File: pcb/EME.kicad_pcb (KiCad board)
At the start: 2 copper layers, 42 parts, among them J1 BMP180, J10 Reset, J11 UART0, J12 SPI_CONN, J13 UART2, J14 MQ135, J15 AS5600, J3 SS41, J4 Hoja Mojada, J5 PanelSolar, J6 BH1750, J7 DHT22, J8 Baterias, J9 Jumper, SW1 Enable, U1 LM78M05_TO220, U5 TL082

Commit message: se actualizó la PCB
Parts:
- removed J15: AS5600, Connector_PinHeader_2.54mm:PinHeader_1x05_P2.54mm_Vertical
- added D3: LED, LED_THT:LED_D5.0mm_Clear, F.Cu at (114.8, 93.2)
- added H4: Sujeción, MountingHole:MountingHole_3.2mm_M3_Pad_Via, F.Cu at (127.6, 24.4)
- added J16: OUT, Connector_PinHeader_2.54mm:PinHeader_1x03_P2.54mm_Vertical, F.Cu at (45.2, 69.3)
- added J17: OE, Connector_PinHeader_2.54mm:PinHeader_1x03_P2.54mm_Vertical, F.Cu at (39.0, 64.0)
- added J18: GPIO's, Connector_PinHeader_2.54mm:PinHeader_1x05_P2.54mm_Vertical, F.Cu at (84.8, 31.6)
- added J19: I2C, Connector_PinHeader_2.54mm:PinHeader_1x05_P2.54mm_Vertical, F.Cu at (108.5, 25.7)
- added J2: ReedSwitchX8, Connector_PinHeader_2.54mm:PinHeader_1x09_P2.54mm_Vertical, F.Cu at (35.9, 38.9)
- added J20: Jumper, Connector_PinHeader_2.54mm:PinHeader_1x02_P2.54mm_Vertical, F.Cu at (117.2, 88.1)
- added Q1: IRF540N, Package_TO_SOT_THT:TO-220-3_Vertical, F.Cu at (68.8, 89.5)
- added Q2: IRF540N, Package_TO_SOT_THT:TO-220-3_Vertical, F.Cu at (98.7, 27.0)
- added R10: 10k, Resistor_THT:R_Axial_DIN0207_L6.3mm_D2.5mm_P10.16mm_Horizontal, F.Cu at (42.4, 43.9)
- added R11: 10k, Resistor_THT:R_Axial_DIN0207_L6.3mm_D2.5mm_P10.16mm_Horizontal, F.Cu at (63.6, 57.0)
- added R12: 10k, Resistor_THT:R_Axial_DIN0207_L6.3mm_D2.5mm_P10.16mm_Horizontal, F.Cu at (45.4, 48.1)
- added R13: 10k, Resistor_THT:R_Axial_DIN0207_L6.3mm_D2.5mm_P10.16mm_Horizontal, F.Cu at (39.2, 50.9)
- added R14: 10k, Resistor_THT:R_Axial_DIN0207_L6.3mm_D2.5mm_P10.16mm_Horizontal, F.Cu at (42.4, 52.8)
- added R15: 10k, Resistor_THT:R_Axial_DIN0207_L6.3mm_D2.5mm_P10.16mm_Horizontal, F.Cu at (54.2, 69.2)
- added R17: 1k, Resistor_THT:R_Axial_DIN0207_L6.3mm_D2.5mm_P10.16mm_Horizontal, F.Cu at (73.5, 87.0)
- added R18: 4k7, Resistor_THT:R_Axial_DIN0207_L6.3mm_D2.5mm_P10.16mm_Horizontal, F.Cu at (70.0, 76.6)
- added R19: 4k7, Resistor_THT:R_Axial_DIN0207_L6.3mm_D2.5mm_P10.16mm_Horizontal, F.Cu at (78.5, 63.9)
- added R20: 1k, Resistor_THT:R_Axial_DIN0207_L6.3mm_D2.5mm_P10.16mm_Horizontal, F.Cu at (88.7, 70.2)
- added R21: 4k7, Resistor_THT:R_Axial_DIN0207_L6.3mm_D2.5mm_P10.16mm_Horizontal, F.Cu at (94.5, 28.2)
- added R22: 4k7, Resistor_THT:R_Axial_DIN0207_L6.3mm_D2.5mm_P10.16mm_Horizontal, F.Cu at (94.5, 25.1)
- added R23: 4k7, Resistor_THT:R_Axial_DIN0207_L6.3mm_D2.5mm_P10.16mm_Horizontal, F.Cu at (99.7, 35.5)
- added R24: 1k, Resistor_THT:R_Axial_DIN0207_L6.3mm_D2.5mm_P10.16mm_Horizontal, F.Cu at (120.5, 77.9)
- added R8: 10k, Resistor_THT:R_Axial_DIN0207_L6.3mm_D2.5mm_P10.16mm_Horizontal, F.Cu at (59.2, 53.7)
- added R9: 10k, Resistor_THT:R_Axial_DIN0207_L6.3mm_D2.5mm_P10.16mm_Horizontal, F.Cu at (39.4, 41.5)
- added U3: 74HC251, Package_DIP:DIP-16_W7.62mm_LongPads, F.Cu at (48.5, 47.8)
- H1, H2, H3: value Sujeción GND -> Sujeción
- J11: value UART0 -> UART2; footprint Connector_PinHeader_2.54mm:PinHeader_1x04_P2.54mm_Vertical -> Connector_PinHeader_2.54mm:PinHeader_1x05_P2.54mm_Vertical
- J13: value UART2 -> UART0; footprint Connector_PinHeader_2.54mm:PinHeader_1x04_P2.54mm_Vertical -> Connector_PinHeader_2.54mm:PinHeader_1x05_P2.54mm_Vertical
- J5: footprint TerminalBlock_Phoenix:TerminalBlock_Phoenix_MPT-0,5-2-2.54_1x02_P2.54mm_Horizontal -> TerminalBlock_Phoenix:TerminalBlock_Phoenix_PT-1,5-2-3.5-H_1x02_P3.50mm_Horizontal
- J8: footprint TerminalBlock_Phoenix:TerminalBlock_Phoenix_MPT-0,5-2-2.54_1x02_P2.54mm_Horizontal -> TerminalBlock_Phoenix:TerminalBlock_Phoenix_PT-1,5-2-5.0-H_1x02_P5.00mm_Horizontal
- moved H1 264.2 mm to (37.7, 24.5)
- moved R1 233.2 mm to (41.6, 73.8), turned to -90 degrees
- moved C5 218.1 mm to (40.1, 86.4), turned to 180 degrees
- moved RV1 217.3 mm to (35.9, 76.8)
- moved U5 217.0 mm to (44.9, 75.9)
- moved R2 216.9 mm to (55.8, 73.3)
- moved R4 213.3 mm to (42.8, 86.3)
- moved J3 212.7 mm to (51.1, 90.5)
- moved C7 209.6 mm to (58.8, 81.0), turned to 0 degrees
- moved R16 205.5 mm to (59.9, 30.1)
- moved J6 204.1 mm to (70.4, 33.9), turned to 180 degrees
- moved J1 196.3 mm to (74.9, 23.8), turned to 0 degrees
- moved J4 196.0 mm to (51.6, 26.8)
- moved J14 192.3 mm to (45.8, 33.7), turned to 180 degrees
- moved SW1 191.7 mm to (67.0, 25.5), turned to -90 degrees
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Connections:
- C5 pad 2: GNDREF -> GND_G1
- C6 pad 2: GNDREF -> GND_G1
- C7 pad 2: GNDREF -> GND_G1
- C9 pad 1: Net-(J10-Pin_2) -> Rest
- J1 pad 2: SDA -> SCL
- J1 pad 3: SCL -> SDA
- J1 pad 4: GNDREF -> GND_G1
- J10 pad 2: Net-(J10-Pin_2) -> Rest
- J11 pad 1: +3.3V -> GND_G2
- J11 pad 2: Net-(J11-Pin_2) -> RX2
- J11 pad 3: Net-(J11-Pin_3) -> TX2
- J11 pad 4: GNDREF -> +5V
- J12 pad 1: GNDREF -> SS
- J12 pad 2: Net-(J12-Pin_2) -> SCK
- J12 pad 3: Net-(J12-Pin_3) -> MOSI
- J12 pad 4: Net-(J12-Pin_4) -> MISO
- J12 pad 5: Net-(J12-Pin_5) -> GND_G2
- J12 pad 6: +3.3V -> +5V
- J12 pad 7: Net-(J12-Pin_7) -> +3.3V
- J13 pad 1: +3.3V -> GND_G2
- J13 pad 2: Net-(J13-Pin_2) -> RX0
- J13 pad 3: Net-(J13-Pin_3) -> TX0
- J13 pad 4: GNDREF -> +5V
- J14 pad 3: GNDREF -> GND_G1
- J3 pad 2: GNDREF -> GND_G1
- J4 pad 3: GNDREF -> GND_G1
- J6 pad 2: GNDREF -> GND_G1
- J6 pad 3: SCL -> SDA
- J6 pad 4: SDA -> SCL
- J7 pad 4: GNDREF -> GND_G1
- R16 pad 1: +3.3V -> Rest
- R16 pad 2: Net-(J10-Pin_2) -> +3.3V
- R4 pad 1: Net-(J3-Pin_3) -> Net-(U5A-+)
- R4 pad 2: Net-(U5A-+) -> Net-(J3-Pin_3)
- R5 pad 1: SDA -> SCL
- R6 pad 1: SCL -> SDA
- RV1 pad 3: GNDREF -> GND_G1
- SW1 pad 2: Net-(J10-Pin_2) -> Rest
- U2 pad 1: Net-(J10-Pin_2) -> Rest
- U2 pad 10: unconnected-(U2-D27/ADC2_7/T7/~-Pad10) -> G2
- U2 pad 11: unconnected-(U2-D14/ADC2_6/HSPI_CLK/T6/~-Pad11) -> G1
- U2 pad 12: unconnected-(U2-D12/ADC2_5/HSPI_Q/T5/~-Pad12) -> GPIO12
- U2 pad 13: unconnected-(U2-D13/ADC2_4/HSPI_ID/T4/~-Pad13) -> GPIO13
- U2 pad 20: Net-(J12-Pin_2) -> GPIO4
- U2 pad 21: Net-(J13-Pin_3) -> RX2
- U2 pad 22: Net-(J13-Pin_2) -> TX2
- U2 pad 23: Net-(J12-Pin_3) -> SS
- U2 pad 24: Net-(J12-Pin_4) -> SCK
- U2 pad 25: Net-(J12-Pin_5) -> MISO
- U2 pad 27: Net-(J11-Pin_2) -> RX0
- U2 pad 28: Net-(J11-Pin_3) -> TX0
- U2 pad 30: Net-(J12-Pin_7) -> MOSI
- U2 pad 6: Net-(J15-Pin_1) -> S0
- U2 pad 7: unconnected-(U2-D33/ADC1_5/T8/~-Pad7) -> S1
- U2 pad 8: unconnected-(U2-D25/ADC2_8/DAC1/~-Pad8) -> S2
- U2 pad 9: unconnected-(U2-D26/ADC2_9/DAC2/~-Pad9) -> Y
- U5 pad 4: GNDREF -> GND_G1
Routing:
- net +3.3V: track 276.4 -> 370.3 mm, vias 10 -> 8
- net GNDREF: track 17.4 -> 91.4 mm, vias 4 -> 8
- net +5V: track 86.0 -> 155.9 mm, vias 0 -> 4
- net GPIO13: track 0.00 -> 67.8 mm
- net GPIO12: track 0.00 -> 60.5 mm
- net GPIO4: track 0.00 -> 55.7 mm
- net Rest: track 0.00 -> 55.1 mm
- net DHT22: track 14.4 -> 63.5 mm, vias 0 -> 2
- net Net-(Q2-G): track 0.00 -> 48.8 mm
- net Net-(J12-Pin_7): track 45.0 -> 0.00 mm
- net Net-(J2-Pin_4): track 0.00 -> 44.8 mm, vias 0 -> 4
- net Net-(J2-Pin_1): track 0.00 -> 42.4 mm
- net SS: track 0.00 -> 40.0 mm
- net SCK: track 0.00 -> 36.4 mm
- net MQ135_Dg: track 8.42 -> 44.6 mm
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- added copper zone on B.Cu, net GND_G1
- added copper zone on B.Cu, net GND_G2
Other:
- board outline added: 100 x 78 mm
- board text added: "EMETec UM"
- board text added: "v:1.8 f:21/10/24"
- board text removed: "EME ETec UM"
- board text removed: "v:1.0 f:16/06/24"

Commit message: se actualizó la PCB
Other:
- board text added: "v:1.8.2 f:27/10/24"
- board text removed: "v:1.8 f:21/10/24"

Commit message: update main
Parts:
- J5: footprint TerminalBlock_Phoenix:TerminalBlock_Phoenix_PT-1,5-2-3.5-H_1x02_P3.50mm_Horizontal -> TerminalBlock_Phoenix:TerminalBlock_Phoenix_PT-1,5-2-5.0-H_1x02_P5.00mm_Horizontal
- moved J12 3.40 mm to (128.9, 40.0)
- moved J5 0.76 mm to (127.5, 51.5)
- moved C3 0.75 mm to (121.0, 91.0)
- moved C4 0.33 mm to (116.2, 78.5)
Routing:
- net MISO: track 32.1 -> 34.6 mm
- net SCK: track 36.4 -> 38.6 mm
- net SS: track 40.0 -> 42.1 mm
- net MOSI: track 30.9 -> 32.9 mm
- net GNDREF: track 91.4 -> 90.2 mm
- net +3.3V: track 370.3 -> 371.3 mm
- net +5V: track 155.9 -> 156.9 mm
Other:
- board text added: "f:02/11/24"
- board text added: "v:1.8.3"
- board text removed: "v:1.8.2 f:27/10/24"

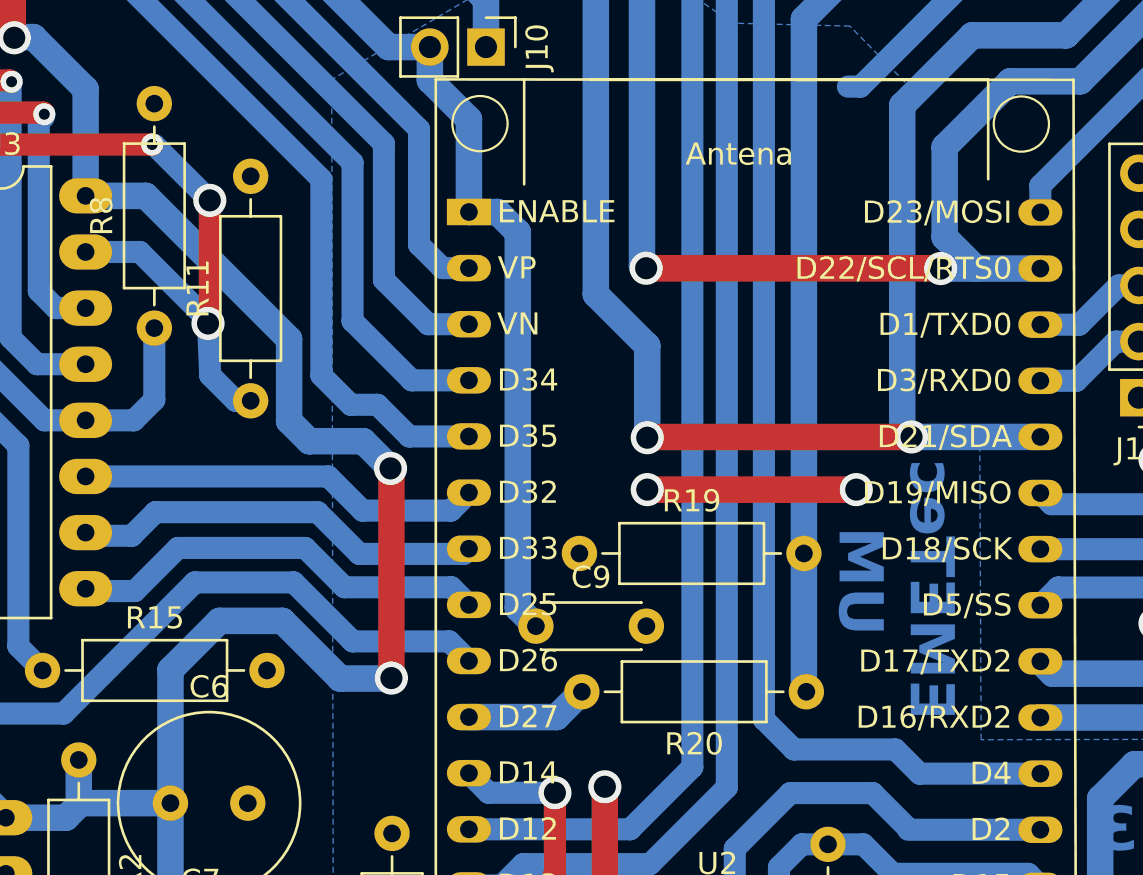
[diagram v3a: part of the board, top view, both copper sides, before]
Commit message: Se actualizó PCB y se agregó funcionalidad de sensor lluvia, veleta y anemómetro
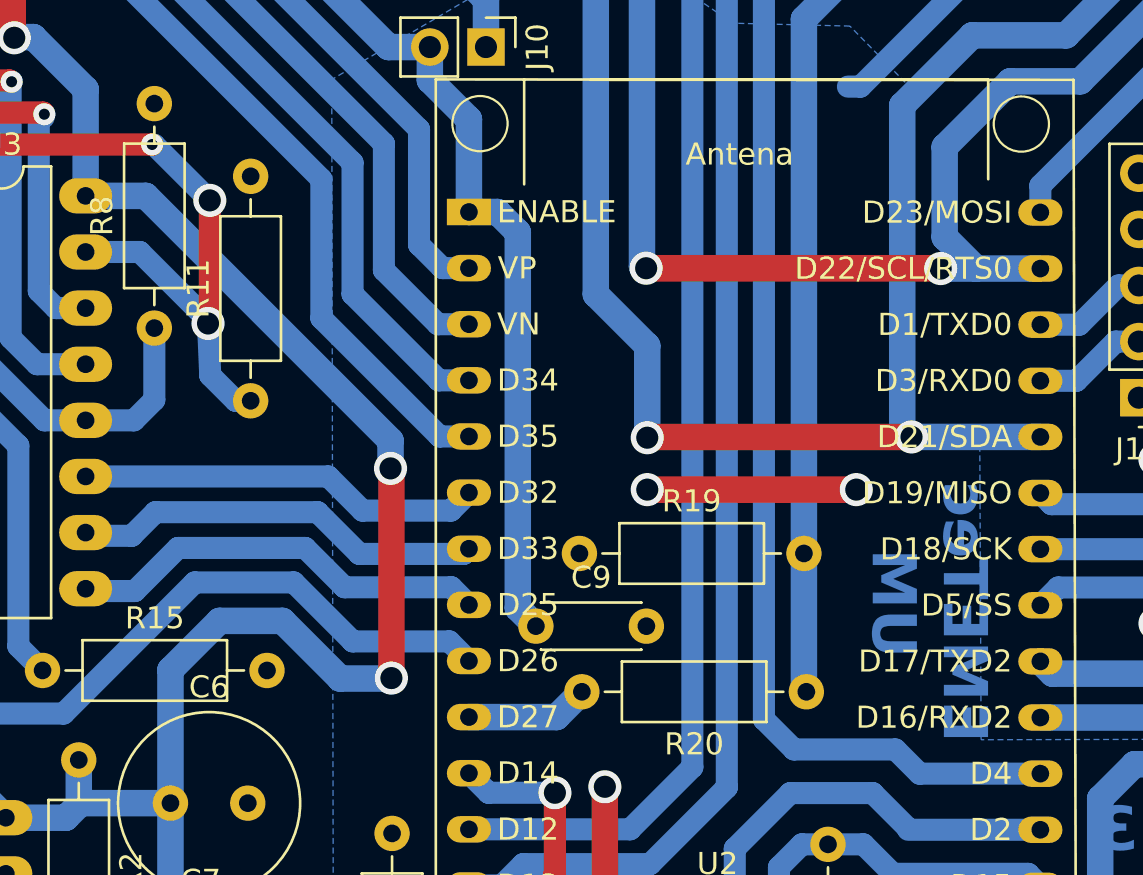
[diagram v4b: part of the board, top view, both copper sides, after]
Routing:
- net MQ135_An: track 43.2 -> 41.7 mm
- net +3.3V: track 371.3 -> 369.9 mm
- net MQ135_Dg: track 44.6 -> 43.9 mm

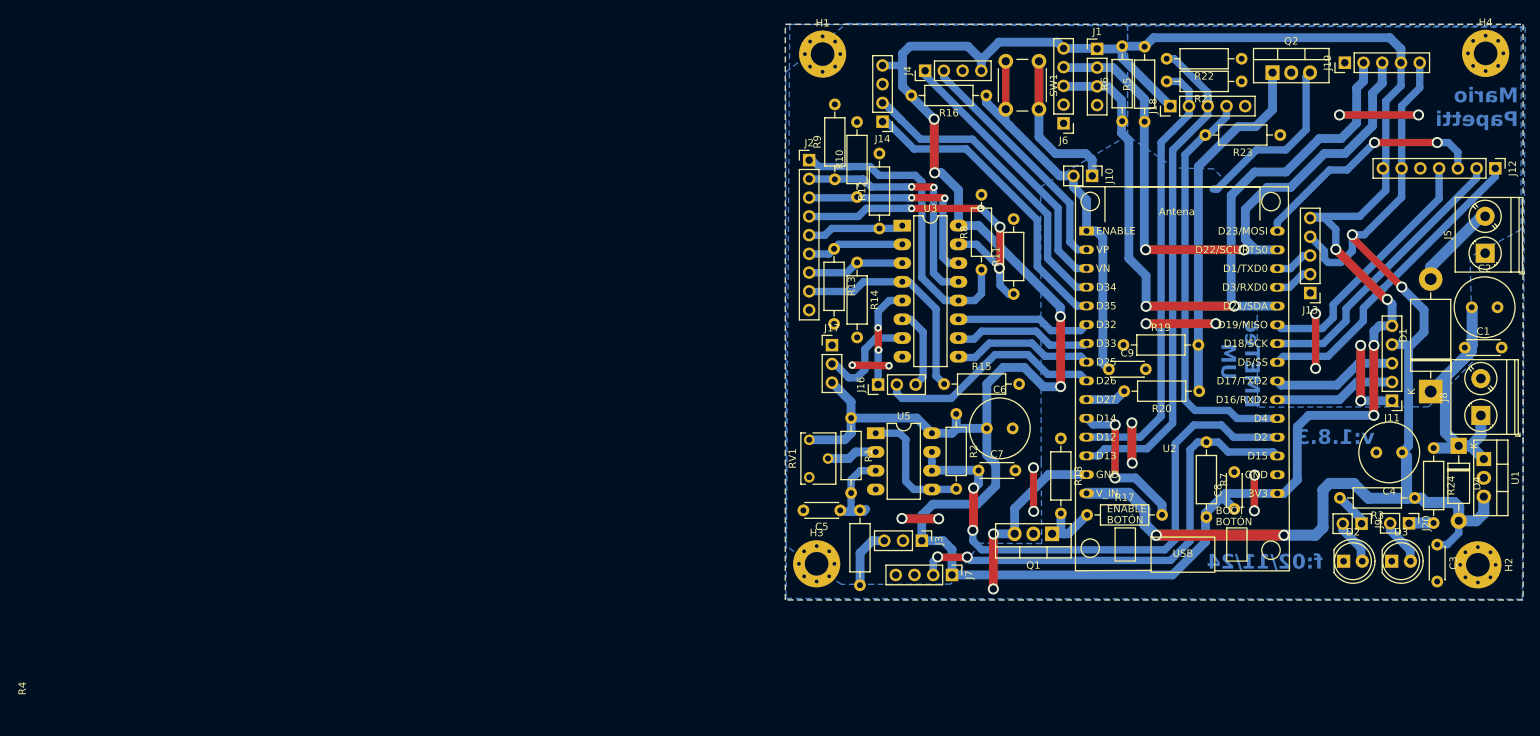
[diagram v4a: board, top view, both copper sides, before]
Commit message: Nueva versión de la PCB, se saca a parte veleta y anemómetro en placas aparte con los sensores
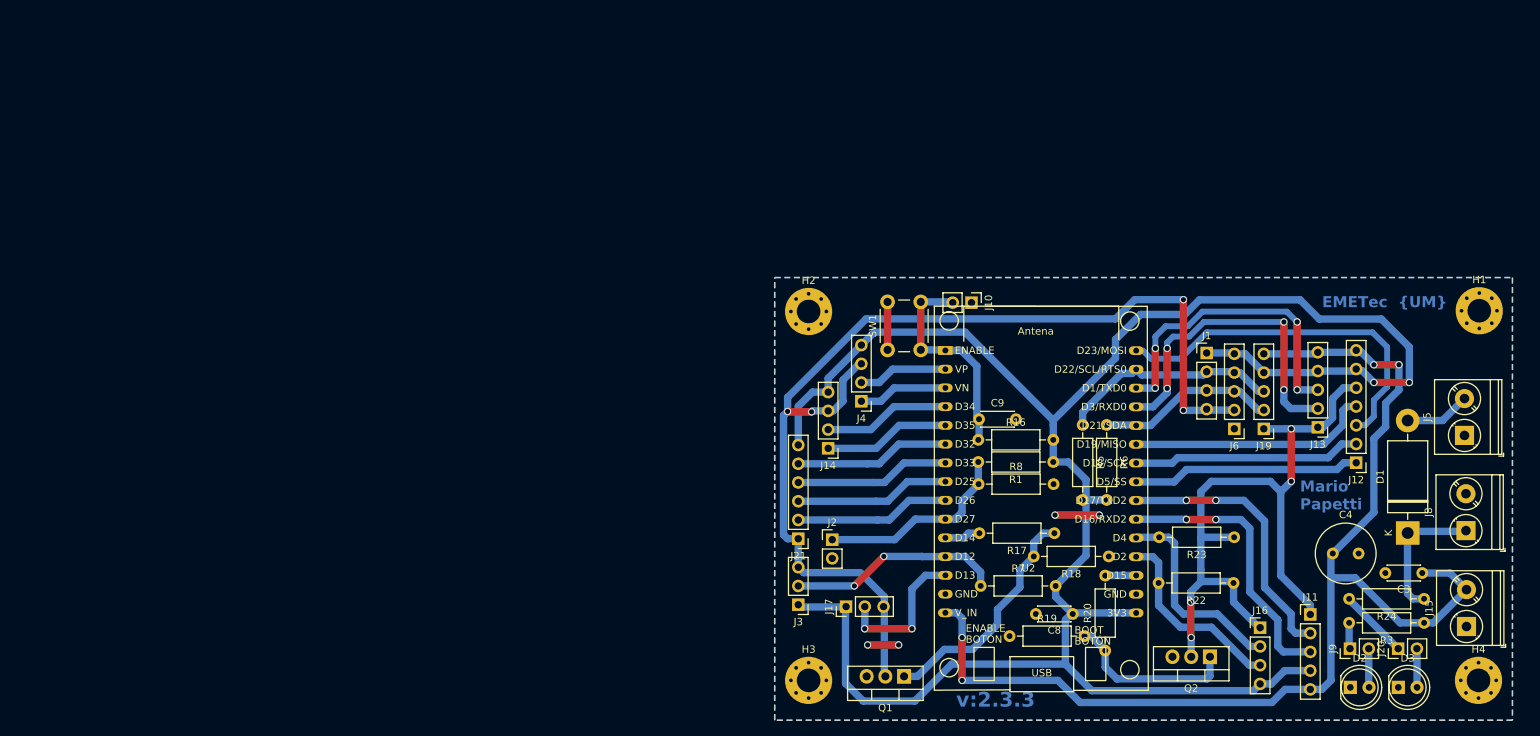
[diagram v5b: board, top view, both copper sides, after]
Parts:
- removed C1, C5, C7: 104, Capacitor_THT:C_Disc_D4.3mm_W1.9mm_P5.00mm
- removed C2, C6: 220uF, Capacitor_THT:C_Radial_D8.0mm_H11.5mm_P3.50mm
- removed D4: 1N4007, Diode_THT:D_DO-41_SOD81_P10.16mm_Horizontal
- removed J18: GPIO's, Connector_PinHeader_2.54mm:PinHeader_1x05_P2.54mm_Vertical
- removed J7: DHT22, Connector_PinHeader_2.54mm:PinHeader_1x04_P2.54mm_Vertical
- removed R10, R11, R12, R13, R14, R15, R2, R9: 10k, Resistor_THT:R_Axial_DIN0207_L6.3mm_D2.5mm_P10.16mm_Horizontal
- removed R21: 4k7, Resistor_THT:R_Axial_DIN0207_L6.3mm_D2.5mm_P10.16mm_Horizontal
- removed R4: 100, Resistor_THT:R_Axial_DIN0207_L6.3mm_D2.5mm_P10.16mm_Horizontal
- removed RV1: 100k, Potentiometer_THT:Potentiometer_Bourns_3266W_Vertical
- removed U1: LM78M05_TO220, Package_TO_SOT_THT:TO-220-3_Vertical
- removed U3: 74HC251, Package_DIP:DIP-16_W7.62mm_LongPads
- removed U5: TL082, Package_DIP:DIP-8_W7.62mm_LongPads
- added J15: 5v, TerminalBlock_Phoenix:TerminalBlock_Phoenix_PT-1,5-2-5.0-H_1x02_P5.00mm_Horizontal, F.Cu at (125.0, 102.1)
- added J21: veleta, Connector_PinHeader_2.54mm:PinHeader_1x06_P2.54mm_Vertical, F.Cu at (34.4, 90.2)
- J16: value OUT -> GPIO's; footprint Connector_PinHeader_2.54mm:PinHeader_1x03_P2.54mm_Vertical -> Connector_PinHeader_2.54mm:PinHeader_1x04_P2.54mm_Vertical
- J17: value OE -> Anemómetro
- J2: value ReedSwitchX8 -> volti; footprint Connector_PinHeader_2.54mm:PinHeader_1x09_P2.54mm_Vertical -> Connector_PinHeader_2.54mm:PinHeader_1x02_P2.54mm_Vertical
- J3: value SS41 -> DHT22
- R1: value 1k -> 4k7
- R8: value 10k -> 4k7
- moved H2 97.0 mm to (35.8, 59.4), turned to 0 degrees
- moved H1 95.6 mm to (126.7, 59.3)
- moved H4 85.0 mm to (126.6, 109.4)
- moved Q2 79.6 mm to (90.2, 106.2), turned to 180 degrees
- moved R22 71.1 mm to (93.4, 96.2)
- moved J16 61.4 mm to (97.0, 102.3), turned to 0 degrees
- moved R23 54.9 mm to (93.5, 90.0)
- moved J2 51.5 mm to (39.0, 90.3)
- moved J19 50.8 mm to (97.5, 75.3), turned to 180 degrees
- moved J6 47.4 mm to (93.5, 75.3)
- moved R16 46.7 mm to (58.8, 76.8), turned to 0 degrees
- moved J4 45.6 mm to (43.0, 71.6), turned to 180 degrees
- moved J14 44.9 mm to (38.5, 78.0)
- moved SW1 44.2 mm to (46.5, 64.6), turned to 90 degrees
- moved J12 44.1 mm to (110.0, 79.9), turned to 180 degrees
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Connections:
- J11 pad 2: RX2 -> TX2
- J11 pad 3: TX2 -> RX2
- J11 pad 4: +5V -> +3.3V
- J11 pad 5: +3.3V -> +5V
- J12 pad 6: +5V -> +3.3V
- J12 pad 7: +3.3V -> +5V
- J13 pad 4: +5V -> +3.3V
- J13 pad 5: +3.3V -> +5V
- J16 pad 1: Net-(J16-Pin_1) -> GND_G2
- J16 pad 2: Y -> GPIO4
- J16 pad 3: Net-(J16-Pin_3) -> GPIO13
- J17 pad 1: GND_G1 -> +3.3V
- J17 pad 2: Net-(J17-Pin_2) -> D_hall
- J17 pad 3: +3.3V -> GND_G1
- J2 pad 1: Net-(J2-Pin_1) -> Div
- J2 pad 2: Net-(J2-Pin_2) -> GNDREF
- J3 pad 2: GND_G1 -> DHT22
- J3 pad 3: Net-(J3-Pin_3) -> GND_G1
- R1 pad 2: Net-(U5A-+) -> Div
- R8 pad 1: Net-(J2-Pin_1) -> Div
- R8 pad 2: GND_G1 -> GNDREF
- U2 pad 10: G2 -> Div
- U2 pad 12: GPIO12 -> DHT22
- U2 pad 13: GPIO13 -> D_hall
- U2 pad 18: DHT22 -> G2
- U2 pad 19: D_hall -> GPIO13
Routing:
- net GND_G1: track 16.1 -> 144.6 mm, vias 6 -> 4
- net +3.3V: track 369.9 -> 280.0 mm, vias 8 -> 2
- net SDA: track 100.7 -> 24.4 mm, vias 2 -> 0
- net GNDREF: track 90.2 -> 16.7 mm, vias 8 -> 4
- net GND_G2: track 29.9 -> 95.6 mm, vias 6 -> 4
- net GPIO12: track 60.5 -> 0.00 mm
- net SCL: track 88.5 -> 30.3 mm, vias 2 -> 0
- net D_hall: track 75.8 -> 20.3 mm
- net Net-(J2-Pin_4): track 44.8 -> 0.00 mm, vias 4 -> 0
- net Net-(J2-Pin_1): track 42.4 -> 0.00 mm
- net GPIO13: track 67.8 -> 26.3 mm
- net RX0: track 5.19 -> 44.6 mm, vias 0 -> 4
- net TX0: track 5.19 -> 42.8 mm, vias 0 -> 4
- net DHT22: track 63.7 -> 29.1 mm
- net Net-(J2-Pin_2): track 32.5 -> 0.00 mm, vias 2 -> 0
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- removed copper zone on B.Cu, net GND_G1
- removed copper zone on B.Cu, net GND_G2
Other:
- board size 100 x 78 mm -> 100 x 60 mm
- board text added: "EMETec {UM}"
- board text added: "v:2.3.3"
- board text removed: "EMETec UM"
- board text removed: "f:02/11/24"
- board text removed: "v:1.8.3"
